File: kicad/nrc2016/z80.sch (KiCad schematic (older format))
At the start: 11 parts, among them P2 CONN_01X02

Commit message: Moved directory layout around to clean things up
.. for future work etc.
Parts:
- LOGO1: footprint ncr2016_logo:nrc2016_top_logo_1600 -> nrc2016_logo:nrc2016_top_logo_1600
- LOGO2: footprint ncr2016_logo:nrc2016_bottom_logo_600_v2 -> nrc2016_logo:nrc2016_bottom_logo_600_v2
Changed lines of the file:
@@
 F 0 "LOGO1" H 3050 7450 60  0000 C CNN
 F 1 "FrontLogo" H 2950 7800 60  0000 C CNN
-F 2 "ncr2016_logo:nrc2016_top_logo_1600" H 2700 7500 60  0001 C CNN
+F 2 "nrc2016_logo:nrc2016_top_logo_1600" H 2700 7500 60  0001 C CNN
 F 3 "" H 2700 7500 60  0000 C CNN
 	1    2700 7500
@@
 F 0 "LOGO2" H 3750 7450 60  0000 C CNN
 F 1 "BackLogo" H 3650 7800 60  0000 C CNN
-F 2 "ncr2016_logo:nrc2016_bottom_logo_600_v2" H 3400 7500 60  0001 C CNN
+F 2 "nrc2016_logo:nrc2016_bottom_logo_600_v2" H 3400 7500 60  0001 C CNN
 F 3 "" H 3400 7500 60  0000 C CNN
 	1    3400 7500

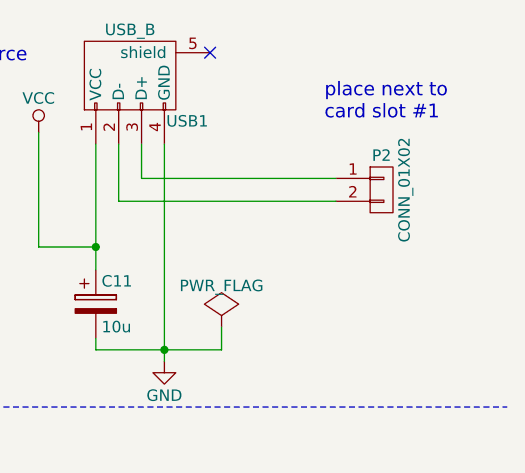
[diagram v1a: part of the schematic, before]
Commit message: Update nrc2016 schema and PCB to use new library symbols
I've added proper schematic symbols for the pre-defined bus sockets to
stop confusion and error by just using the generic "library" socket
component and then relying on the net names to define the pins. Screwed
me once with the VCC and GND switch around, not going to happen again.
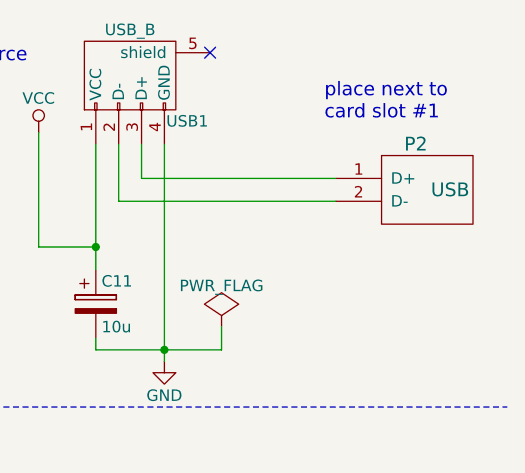
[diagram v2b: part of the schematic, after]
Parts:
- removed P2: CONN_01X02, Socket_Strips:Socket_Strip_Straight_1x02, symbol CONN_01X02
- added P2: USB, Socket_Strips:Socket_Strip_Straight_1x02, symbol USB
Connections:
- net at USB1.2 (D-): now also P2.2 (D-)
- net at USB1.3 (D+): now also P2.1 (D+)
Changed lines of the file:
@@
 LIBS:valves
 LIBS:Zilog
-LIBS:microchip_pic18mcu
-LIBS:6850
 LIBS:nrc2016
 LIBS:atf16v8cv
-LIBS:62256
-LIBS:mcp2221a
 LIBS:z80-cache
 EELAYER 25 0
@@
 Wire Wire Line
 	9450 1300 9450 1050
-$Comp
-L CONN_01X02 P2
-U 1 1 57A5699E
-P 10600 1250
-F 0 "P2" H 10600 1400 50  0000 C CNN
-F 1 "CONN_01X02" V 10700 1250 50  0000 C CNN
-F 2 "Socket_Strips:Socket_Strip_Straight_1x02" H 10600 1250 50  0001 C CNN
-F 3 "" H 10600 1250 50  0000 C CNN
-	1    10600 1250
-	1    0    0    -1
-$EndComp
 Text Notes 10350 950  0    60   ~ 0
 place next to\ncard slot #1
@@
 	1    0    0    -1
 $EndComp
+$Comp
+L USB P2
+U 1 1 57D437FB
+P 10600 800
+F 0 "P2" H 10750 550 60  0000 C CNN
+F 1 "USB" H 10900 350 60  0000 C CNN
+F 2 "Socket_Strips:Socket_Strip_Straight_1x02" H 10600 800 60  0001 C CNN
+F 3 "" H 10600 800 60  0000 C CNN
+	1    10600 800
+	1    0    0    -1
+$EndComp

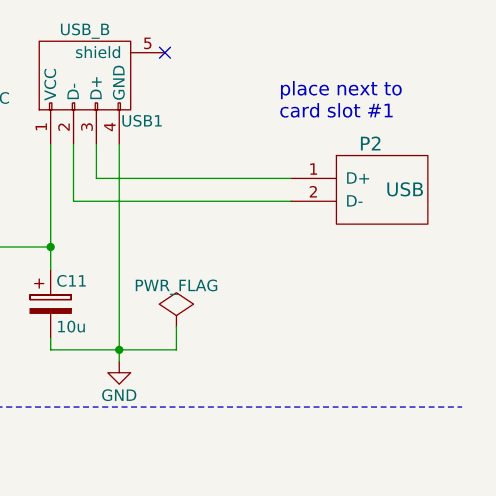
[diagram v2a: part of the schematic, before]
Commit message: More moving things around. Added sockets and pins symbols
Makes it easier for DRC and has hints for the right footprints already.
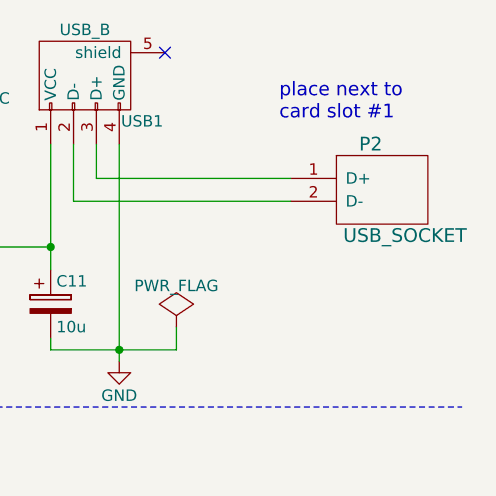
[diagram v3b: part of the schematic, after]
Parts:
- removed P2: USB, Socket_Strips:Socket_Strip_Straight_1x02, symbol USB
- added P2: USB_SOCKET, Socket_Strips:Socket_Strip_Straight_1x02, symbol USB_SOCKET
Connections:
- net at USB1.2 (D-): now also P2.2 (D-)
- net at USB1.3 (D+): now also P2.1 (D+)
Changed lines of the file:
@@
 $EndComp
 $Comp
-L USB P2
-U 1 1 57D437FB
+L USB_SOCKET P2
+U 1 1 57D45BF2
 P 10600 800
 F 0 "P2" H 10750 550 60  0000 C CNN
-F 1 "USB" H 10900 350 60  0000 C CNN
+F 1 "USB_SOCKET" H 10900 150 60  0000 C CNN
 F 2 "Socket_Strips:Socket_Strip_Straight_1x02" H 10600 800 60  0001 C CNN
 F 3 "" H 10600 800 60  0000 C CNN
